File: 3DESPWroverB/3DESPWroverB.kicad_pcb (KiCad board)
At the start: 2 copper layers, 40 x 40 mm, 18 parts, among them J1 Conn_02x07_Odd_Even, J10 Conn_02x03_Odd_Even, J11 Conn_01x01, J12 Conn_01x01, J13 Conn_01x01, J14 Conn_01x01, J15 Conn_01x01, J16 Conn_01x01, J17 Conn_01x01, J18 Conn_01x01, J2 Conn_01x01, J3 Conn_01x01, J4 Conn_01x01, J5 Conn_01x01, J6 Conn_01x01, J7 Conn_01x01, J8 Conn_01x01, J9 Conn_01x01

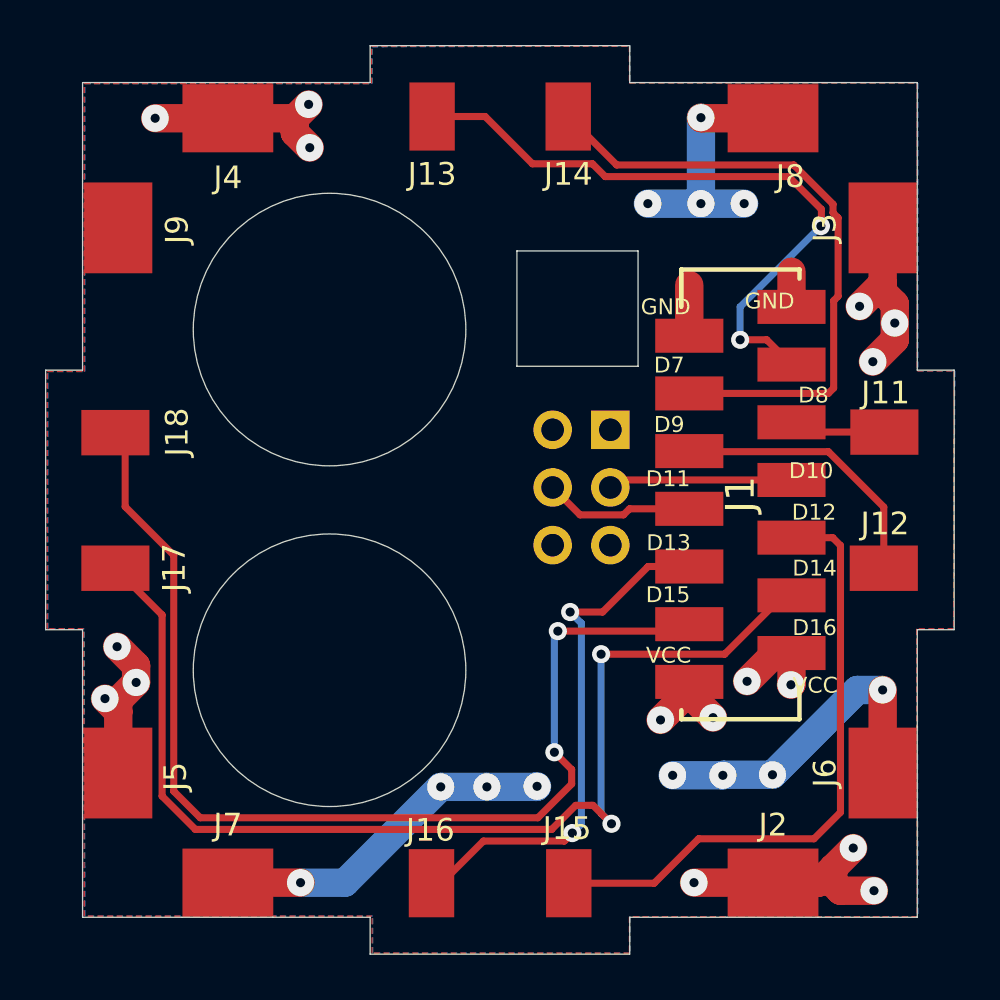
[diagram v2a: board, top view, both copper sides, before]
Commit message: Corrected switching step down power source connections and added mill corner paths
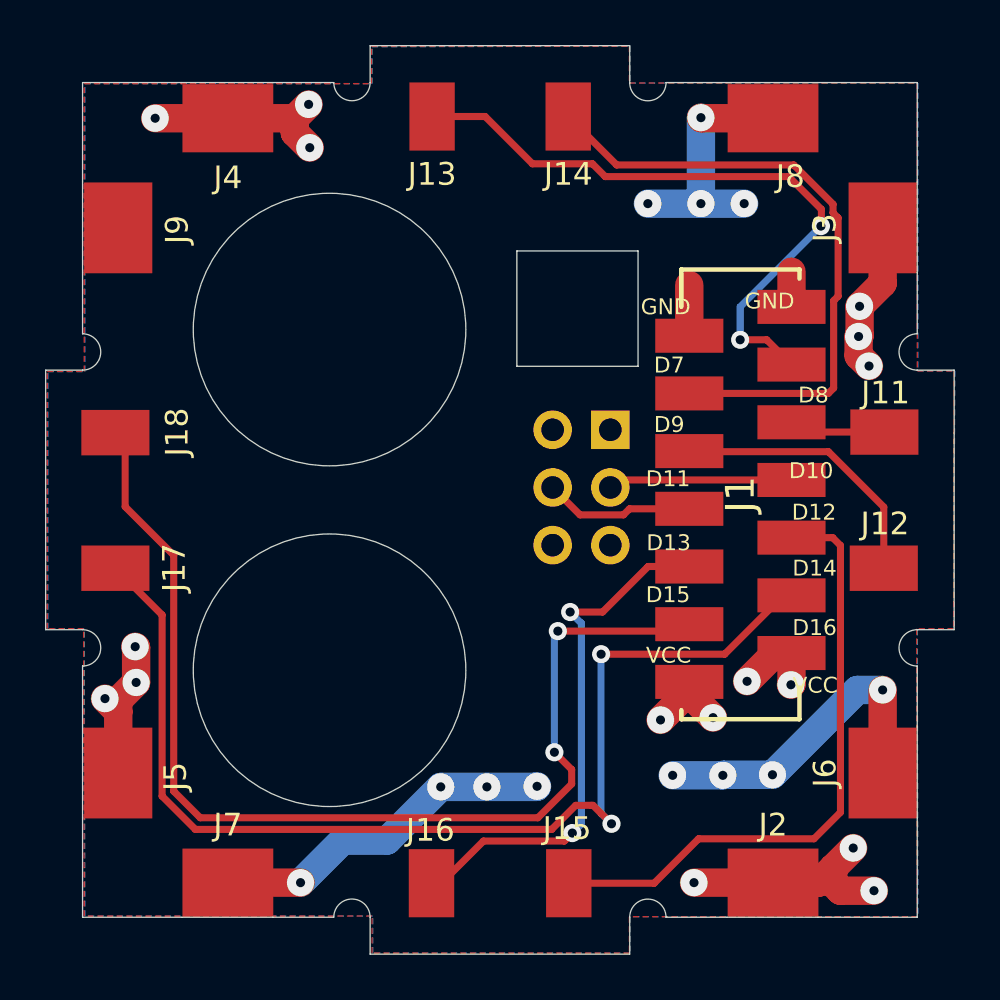
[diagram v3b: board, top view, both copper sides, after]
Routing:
- net VCC: track 41.9 -> 40.4 mm
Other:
- outline, holes or cut-outs redrawn
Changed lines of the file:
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@@
   (general
     (thickness 1.6)
-    (drawings 121)
+    (drawings 129)
     (tracks 167)
     (zones 0)
@@
     )
   )
+  (gr_arc (start 158.192292 75.819) (end 158.992292 75.819) (angle -180) (layer Edge.Cuts) (width 0.02))
+  (gr_arc (start 133.303001 63.958292) (end 133.303001 64.758292) (angle -180) (layer Edge.Cuts) (width 0.02))
+  (gr_arc (start 145.16371 39.07) (end 144.36371 39.07) (angle -180) (layer Edge.Cuts) (width 0.02))
+  (gr_arc (start 145.163715 75.816) (end 145.963715 75.819) (angle -180.2148582) (layer Edge.Cuts) (width 0.02))
+  (gr_arc (start 133.303 50.93) (end 133.3 51.73) (angle -180.2148582) (layer Edge.Cuts) (width 0.02))
+  (gr_arc (start 158.192286 39.072001) (end 157.392286 39.069001) (angle -180.2148582) (layer Edge.Cuts) (width 0.02))
+  (gr_arc (start 170.05 63.958287) (end 170.053 63.158287) (angle -180.2148582) (layer Edge.Cuts) (width 0.02))
+  (gr_arc (start 170.05 50.93) (end 170.053 50.13) (angle -180.2148582) (layer Edge.Cuts) (width 0.02))
   (gr_text GND (at 151.5618 54.229 180) (layer B.SilkS)
     (effects (font (size 0.7 0.7) (thickness 0.15)) (justify mirror))
@@
   (gr_line (start 136.303001 47.444001) (end 136.303001 43.444001) (layer Dwgs.User) (width 0.2))
   (gr_line (start 133.303001 39.069001) (end 137.678001 39.069001) (layer Edge.Cuts) (width 0.02))
-  (gr_line (start 133.303001 51.729715) (end 133.303001 47.444001) (layer Edge.Cuts) (width 0.02))
+  (gr_line (start 133.303001 50.13) (end 133.303001 47.444001) (layer Edge.Cuts) (width 0.02))
   (gr_line (start 137.678001 42.069001) (end 141.678001 42.069001) (layer Dwgs.User) (width 0.2))
-  (gr_line (start 157.392286 39.069001) (end 161.678 39.069001) (layer Edge.Cuts) (width 0.02))
+  (gr_line (start 158.992292 39.069001) (end 161.678 39.069001) (layer Edge.Cuts) (width 0.02))
   (gr_line (start 137.678001 39.069001) (end 137.678001 42.069001) (layer Dwgs.User) (width 0.2))
   (gr_line (start 131.678001 63.158286) (end 131.678001 51.729715) (layer Edge.Cuts) (width 0.02))
   (gr_line (start 131.678001 51.729715) (end 133.303001 51.729715) (layer Edge.Cuts) (width 0.02))
-  (gr_line (start 141.678001 39.069001) (end 145.963716 39.069001) (layer Edge.Cuts) (width 0.02))
+  (gr_line (start 141.678001 39.069001) (end 144.36371 39.069001) (layer Edge.Cuts) (width 0.02))
   (gr_line (start 136.303001 43.444001) (end 133.303001 43.444001) (layer Dwgs.User) (width 0.2))
   (gr_line (start 157.392286 37.444001) (end 157.392286 39.069001) (layer Edge.Cuts) (width 0.02))
@@
   (gr_line (start 167.053 43.444001) (end 167.053 47.444001) (layer Dwgs.User) (width 0.2))
   (gr_line (start 161.678 39.069001) (end 161.678 42.069001) (layer Dwgs.User) (width 0.2))
-  (gr_line (start 133.303001 67.444001) (end 133.303001 63.158286) (layer Edge.Cuts) (width 0.02))
-  (gr_line (start 170.053 51.729715) (end 171.678 51.729715) (layer Edge.Cuts) (width 0.02))
+  (gr_line (start 133.303001 67.444001) (end 133.303001 64.758292) (layer Edge.Cuts) (width 0.02))
+  (gr_line (start 170.05 51.73) (end 171.678 51.729715) (layer Edge.Cuts) (width 0.02))
   (gr_line (start 136.303002 67.444001) (end 133.303001 67.444001) (layer Dwgs.User) (width 0.2))
   (gr_line (start 167.053 67.444001) (end 167.053 71.444) (layer Dwgs.User) (width 0.2))
@@
   (gr_line (start 137.678001 72.819) (end 137.678001 75.819) (layer Dwgs.User) (width 0.2))
   (gr_line (start 141.678001 72.819) (end 137.678001 72.819) (layer Dwgs.User) (width 0.2))
-  (gr_line (start 145.963715 75.819) (end 141.678001 75.819) (layer Edge.Cuts) (width 0.02))
+  (gr_line (start 144.363709 75.819) (end 141.678001 75.819) (layer Edge.Cuts) (width 0.02))
   (gr_line (start 157.392286 77.444) (end 145.963715 77.444) (layer Edge.Cuts) (width 0.02))
-  (gr_line (start 161.678 75.819) (end 157.392286 75.819) (layer Edge.Cuts) (width 0.02))
+  (gr_line (start 161.678 75.819) (end 158.992292 75.819) (layer Edge.Cuts) (width 0.02))
   (gr_line (start 165.678 72.819) (end 161.678 72.819) (layer Dwgs.User) (width 0.2))
   (gr_line (start 161.678 42.069001) (end 165.678 42.069001) (layer Dwgs.User) (width 0.2))
@@
   (gr_line (start 171.678 51.729715) (end 171.678 63.158286) (layer Edge.Cuts) (width 0.02))
   (gr_line (start 171.678 63.158286) (end 170.078 63.158287) (layer Edge.Cuts) (width 0.02))
-  (gr_line (start 170.053 47.444001) (end 170.053 51.729715) (layer Edge.Cuts) (width 0.02))
+  (gr_line (start 170.053 47.444001) (end 170.053 50.13) (layer Edge.Cuts) (width 0.02))
   (gr_line (start 170.053 39.069001) (end 170.053 43.444001) (layer Edge.Cuts) (width 0.02))
   (gr_line (start 170.053 75.819) (end 165.678 75.819) (layer Edge.Cuts) (width 0.02))
-  (gr_line (start 170.053 63.158287) (end 170.053 67.444001) (layer Edge.Cuts) (width 0.02))
+  (gr_line (start 170.053 64.758293) (end 170.053 67.444001) (layer Edge.Cuts) (width 0.02))
   (gr_line (start 170.053 55.444001) (end 170.053 53.444001) (layer Dwgs.User) (width 0.2))
   (gr_line (start 167.053 53.444001) (end 167.053 55.444001) (layer Dwgs.User) (width 0.2))
@@
   (segment (start 168.529 47.9044) (end 167.513 48.9204) (width 1.25) (layer F.Cu) (net 1))
   (segment (start 168.529 45.466) (end 168.529 47.9044) (width 1.25) (layer F.Cu) (net 1))
-  (via (at 169.0624 49.657) (size 1.2) (drill 0.4) (layers F.Cu B.Cu) (net 1))
-  (segment (start 169.0624 48.816) (end 169.0624 49.657) (width 1.25) (layer F.Cu) (net 1))
-  (segment (start 168.529 48.2826) (end 169.0624 48.816) (width 1.25) (layer F.Cu) (net 1))
-  (segment (start 168.529 47.9044) (end 168.529 48.2826) (width 1.25) (layer F.Cu) (net 1))
+  (via (at 167.47 50.25) (size 1.2) (drill 0.4) (layers F.Cu B.Cu) (net 1))
   (via (at 143.256 40.0304) (size 1.2) (drill 0.4) (layers F.Cu B.Cu) (net 1))
   (segment (start 142.6464 40.64) (end 143.256 40.0304) (width 1.25) (layer F.Cu) (net 1))
@@
   (via (at 136.4996 40.64) (size 1.2) (drill 0.4) (layers F.Cu B.Cu) (net 1))
   (segment (start 139.7 40.64) (end 136.4996 40.64) (width 1.25) (layer F.Cu) (net 1))
-  (via (at 168.0972 51.3588) (size 1.2) (drill 0.4) (layers F.Cu B.Cu) (net 1))
-  (segment (start 169.0624 50.3936) (end 168.0972 51.3588) (width 1.25) (layer F.Cu) (net 1))
-  (segment (start 169.0624 49.657) (end 169.0624 50.3936) (width 1.25) (layer F.Cu) (net 1))
+  (via (at 167.93 51.55) (size 1.2) (drill 0.4) (layers F.Cu B.Cu) (net 1))
   (via (at 134.2898 66.1924) (size 1.2) (drill 0.4) (layers F.Cu B.Cu) (net 1))
   (segment (start 134.874 66.7766) (end 134.2898 66.1924) (width 1.25) (layer F.Cu) (net 1))
@@
   (segment (start 134.874 66.2686) (end 135.6614 65.4812) (width 1.25) (layer F.Cu) (net 1))
   (segment (start 134.874 66.7766) (end 134.874 66.2686) (width 1.25) (layer F.Cu) (net 1))
-  (via (at 134.8232 63.9064) (size 1.2) (drill 0.4) (layers F.Cu B.Cu) (net 1))
-  (segment (start 135.6614 64.7446) (end 134.8232 63.9064) (width 1.25) (layer F.Cu) (net 1))
-  (segment (start 135.6614 65.4812) (end 135.6614 64.7446) (width 1.25) (layer F.Cu) (net 1))
+  (via (at 135.62 63.9064) (size 1.2) (drill 0.4) (layers F.Cu B.Cu) (net 1))
   (via (at 158.75 67.1322) (size 1.2) (drill 0.4) (layers F.Cu B.Cu) (net 1))
   (segment (start 160.0158 65.8664) (end 158.75 67.1322) (width 1.25) (layer F.Cu) (net 1))
@@
   (segment (start 163.8046 64.1858) (end 162.56 65.4304) (width 1.25) (layer F.Cu) (net 1))
   (segment (start 164.5158 64.1858) (end 163.8046 64.1858) (width 1.25) (layer F.Cu) (net 1))
+  (segment (start 167.513 50.207) (end 167.47 50.25) (width 1.25) (layer F.Cu) (net 1))
+  (segment (start 167.513 48.9204) (end 167.513 50.207) (width 1.25) (layer F.Cu) (net 1))
+  (segment (start 167.47 51.09) (end 167.93 51.55) (width 1.25) (layer F.Cu) (net 1))
+  (segment (start 167.47 50.25) (end 167.47 51.09) (width 1.25) (layer F.Cu) (net 1))
+  (segment (start 135.6614 63.9478) (end 135.62 63.9064) (width 1.25) (layer F.Cu) (net 1))
+  (segment (start 135.6614 65.4812) (end 135.6614 63.9478) (width 1.25) (layer F.Cu) (net 1))
   (segment (start 135.1788 54.9148) (end 134.747 54.483) (width 0.3125) (layer F.Cu) (net 2))
   (segment (start 137.31691 59.880658) (end 135.1788 57.742548) (width 0.3125) (layer F.Cu) (net 2))
@@
   (via (at 142.9004 74.295) (size 1.2) (drill 0.4) (layers F.Cu B.Cu) (net 12))
   (segment (start 139.7 74.295) (end 142.9004 74.295) (width 1.25) (layer F.Cu) (net 12))
-  (segment (start 142.9004 74.295) (end 144.8562 74.295) (width 1.25) (layer B.Cu) (net 12))
   (via (at 149.0726 70.0786) (size 1.2) (drill 0.4) (layers F.Cu B.Cu) (net 12))
-  (segment (start 144.8562 74.295) (end 149.0726 70.0786) (width 1.25) (layer B.Cu) (net 12))
   (via (at 151.1046 70.0786) (size 1.2) (drill 0.4) (layers F.Cu B.Cu) (net 12))
   (segment (start 149.0726 70.0786) (end 151.1046 70.0786) (width 1.25) (layer B.Cu) (net 12))
@@
   (segment (start 160.0158 50.2158) (end 160.0158 47.9848) (width 1.25) (layer F.Cu) (net 12))
   (segment (start 164.5158 48.9458) (end 164.5158 47.3964) (width 1.25) (layer F.Cu) (net 12))
+  (segment (start 142.9004 74.295) (end 144.7554 72.44) (width 1.25) (layer B.Cu) (net 12))
+  (segment (start 146.7112 72.44) (end 149.0726 70.0786) (width 1.25) (layer B.Cu) (net 12))
+  (segment (start 144.7554 72.44) (end 146.7112 72.44) (width 1.25) (layer B.Cu) (net 12))
   (zone (net 12) (net_name GND) (layer F.Cu) (hatch edge 0.508)
     (connect_pads (clearance 0.508))

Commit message: Ordered
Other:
- board text added: "Project Cube, v1.2"
- board text added: "REAL ITU"
- board text removed: "Project Cube, v1.1"
- board text removed: "REAL ITU rodr"
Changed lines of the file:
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@@
       (effects (font (size 1 1) (thickness 0.15)) (justify mirror))
     )
+    (fp_line (start 4.35 1.8) (end -1.8 1.8) (layer B.CrtYd) (width 0.05))
+    (fp_line (start 4.35 -6.85) (end 4.35 1.8) (layer B.CrtYd) (width 0.05))
+    (fp_line (start -1.8 -6.85) (end 4.35 -6.85) (layer B.CrtYd) (width 0.05))
+    (fp_line (start -1.8 1.8) (end -1.8 -6.85) (layer B.CrtYd) (width 0.05))
+    (fp_line (start -1.33 1.33) (end 0 1.33) (layer B.SilkS) (width 0.12))
+    (fp_line (start -1.33 0) (end -1.33 1.33) (layer B.SilkS) (width 0.12))
+    (fp_line (start 1.27 1.33) (end 3.87 1.33) (layer B.SilkS) (width 0.12))
+    (fp_line (start 1.27 -1.27) (end 1.27 1.33) (layer B.SilkS) (width 0.12))
+    (fp_line (start -1.33 -1.27) (end 1.27 -1.27) (layer B.SilkS) (width 0.12))
+    (fp_line (start 3.87 1.33) (end 3.87 -6.41) (layer B.SilkS) (width 0.12))
+    (fp_line (start -1.33 -1.27) (end -1.33 -6.41) (layer B.SilkS) (width 0.12))
+    (fp_line (start -1.33 -6.41) (end 3.87 -6.41) (layer B.SilkS) (width 0.12))
+    (fp_line (start -1.27 0) (end 0 1.27) (layer B.Fab) (width 0.1))
+    (fp_line (start -1.27 -6.35) (end -1.27 0) (layer B.Fab) (width 0.1))
+    (fp_line (start 3.81 -6.35) (end -1.27 -6.35) (layer B.Fab) (width 0.1))
+    (fp_line (start 3.81 1.27) (end 3.81 -6.35) (layer B.Fab) (width 0.1))
     (fp_line (start 0 1.27) (end 3.81 1.27) (layer B.Fab) (width 0.1))
-    (fp_line (start 3.81 1.27) (end 3.81 -6.35) (layer B.Fab) (width 0.1))
-    (fp_line (start 3.81 -6.35) (end -1.27 -6.35) (layer B.Fab) (width 0.1))
-    (fp_line (start -1.27 -6.35) (end -1.27 0) (layer B.Fab) (width 0.1))
-    (fp_line (start -1.27 0) (end 0 1.27) (layer B.Fab) (width 0.1))
-    (fp_line (start -1.33 -6.41) (end 3.87 -6.41) (layer B.SilkS) (width 0.12))
-    (fp_line (start -1.33 -1.27) (end -1.33 -6.41) (layer B.SilkS) (width 0.12))
-    (fp_line (start 3.87 1.33) (end 3.87 -6.41) (layer B.SilkS) (width 0.12))
-    (fp_line (start -1.33 -1.27) (end 1.27 -1.27) (layer B.SilkS) (width 0.12))
-    (fp_line (start 1.27 -1.27) (end 1.27 1.33) (layer B.SilkS) (width 0.12))
-    (fp_line (start 1.27 1.33) (end 3.87 1.33) (layer B.SilkS) (width 0.12))
-    (fp_line (start -1.33 0) (end -1.33 1.33) (layer B.SilkS) (width 0.12))
-    (fp_line (start -1.33 1.33) (end 0 1.33) (layer B.SilkS) (width 0.12))
-    (fp_line (start -1.8 1.8) (end -1.8 -6.85) (layer B.CrtYd) (width 0.05))
-    (fp_line (start -1.8 -6.85) (end 4.35 -6.85) (layer B.CrtYd) (width 0.05))
-    (fp_line (start 4.35 -6.85) (end 4.35 1.8) (layer B.CrtYd) (width 0.05))
-    (fp_line (start 4.35 1.8) (end -1.8 1.8) (layer B.CrtYd) (width 0.05))
     (fp_text user %R (at 1.27 -2.54 270) (layer B.Fab)
       (effects (font (size 1 1) (thickness 0.15)) (justify mirror))
@@
       (effects (font (size 1.27 1.27) (thickness 0.254)))
     )
+    (fp_line (start 9.9 -2.6) (end 8.5 -2.6) (layer F.SilkS) (width 0.2))
+    (fp_line (start 9.9 2.6) (end 9.9 -2.6) (layer F.SilkS) (width 0.2))
+    (fp_line (start 9.5 2.6) (end 9.9 2.6) (layer F.SilkS) (width 0.2))
+    (fp_line (start -9.9 2.6) (end -8.255 2.6) (layer F.SilkS) (width 0.2))
+    (fp_line (start -9.9 -2.6) (end -9.9 2.6) (layer F.SilkS) (width 0.2))
+    (fp_line (start -9.5 -2.6) (end -9.9 -2.6) (layer F.SilkS) (width 0.2))
+    (fp_line (start -10.9 4.75) (end -10.9 -4.75) (layer F.CrtYd) (width 0.1))
+    (fp_line (start 10.9 4.75) (end -10.9 4.75) (layer F.CrtYd) (width 0.1))
+    (fp_line (start 10.9 -4.75) (end 10.9 4.75) (layer F.CrtYd) (width 0.1))
+    (fp_line (start -10.9 -4.75) (end 10.9 -4.75) (layer F.CrtYd) (width 0.1))
+    (fp_line (start -9.9 2.6) (end -9.9 -2.6) (layer F.Fab) (width 0.1))
+    (fp_line (start 9.9 2.6) (end -9.9 2.6) (layer F.Fab) (width 0.1))
+    (fp_line (start 9.9 -2.6) (end 9.9 2.6) (layer F.Fab) (width 0.1))
     (fp_line (start -9.9 -2.6) (end 9.9 -2.6) (layer F.Fab) (width 0.1))
-    (fp_line (start 9.9 -2.6) (end 9.9 2.6) (layer F.Fab) (width 0.1))
-    (fp_line (start 9.9 2.6) (end -9.9 2.6) (layer F.Fab) (width 0.1))
-    (fp_line (start -9.9 2.6) (end -9.9 -2.6) (layer F.Fab) (width 0.1))
-    (fp_line (start -10.9 -4.75) (end 10.9 -4.75) (layer F.CrtYd) (width 0.1))
-    (fp_line (start 10.9 -4.75) (end 10.9 4.75) (layer F.CrtYd) (width 0.1))
-    (fp_line (start 10.9 4.75) (end -10.9 4.75) (layer F.CrtYd) (width 0.1))
-    (fp_line (start -10.9 4.75) (end -10.9 -4.75) (layer F.CrtYd) (width 0.1))
-    (fp_line (start -9.5 -2.6) (end -9.9 -2.6) (layer F.SilkS) (width 0.2))
-    (fp_line (start -9.9 -2.6) (end -9.9 2.6) (layer F.SilkS) (width 0.2))
-    (fp_line (start -9.9 2.6) (end -8.255 2.6) (layer F.SilkS) (width 0.2))
-    (fp_line (start 9.5 2.6) (end 9.9 2.6) (layer F.SilkS) (width 0.2))
-    (fp_line (start 9.9 2.6) (end 9.9 -2.6) (layer F.SilkS) (width 0.2))
-    (fp_line (start 9.9 -2.6) (end 8.5 -2.6) (layer F.SilkS) (width 0.2))
     (fp_text user %R (at 0 0 90) (layer F.Fab)
       (effects (font (size 1.27 1.27) (thickness 0.254)))
@@
     (effects (font (size 0.7 0.7) (thickness 0.15)) (justify mirror))
   )
-  (gr_text "REAL\nITU\nrodr" (at 151.6888 42.2656) (layer B.SilkS)
+  (gr_text "REAL\nITU" (at 151.6888 42.2656) (layer B.SilkS)
     (effects (font (size 1 1) (thickness 0.15)) (justify mirror))
   )
-  (gr_text "Project Cube, v1.1" (at 142.0114 57.4548) (layer B.SilkS)
+  (gr_text "Project Cube, v1.2" (at 142.0114 57.4548) (layer B.SilkS)
     (effects (font (size 1 1) (thickness 0.15)) (justify mirror))
   )
